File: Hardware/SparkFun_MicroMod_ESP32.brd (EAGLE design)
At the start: 22 x 22 mm, 55 parts, among them J1 MICROMOD-2222, Q2 MBT3904DW1T1, U1 W25QXX128MBIT-6X5, U2 ESP32, U4 CP2102N, Y1 40MHz, Y2 32.768kHz

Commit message: v10
- Updated board to v10
- Removed RX and TX test points
- Changed Flash_VDD label to VDD power symbol
- Changed SPI labels to COPI CIPO
- Added vias below antenna
- Moved OSHW logo
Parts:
- removed TP1, TP2: (no value), SparkFun-Connectors:PAD.03X.03
- moved LOGO3 3.68 mm to (16.0, 8.59)
- moved Q2 0.26 mm to (20.0, 9.69)
- moved R18 0.06 mm to (20.0, 11.7)
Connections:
- net 15-SPI_MOSI/SD_CMD renamed 15-SPI_COPI/SD_CMD
- net 2-SPI_MISO/SD_DATA0 renamed 2-SPI_CIPO/SD_DATA0
- net FLASH_VDD renamed VDD
- net U0RXD: no longer TP1.P$1
- net U0TXD: no longer TP2.P$1
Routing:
- net U0TXD: track 18.1 -> 12.5 mm
- net DTR: track 10.1 -> 9.01 mm
- net U0RXD: track 11.0 -> 10.2 mm
- net N$12: track 2.97 -> 3.50 mm
- net GND: vias 67 -> 71
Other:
- board text added: "v10"
- board text removed: "v02"

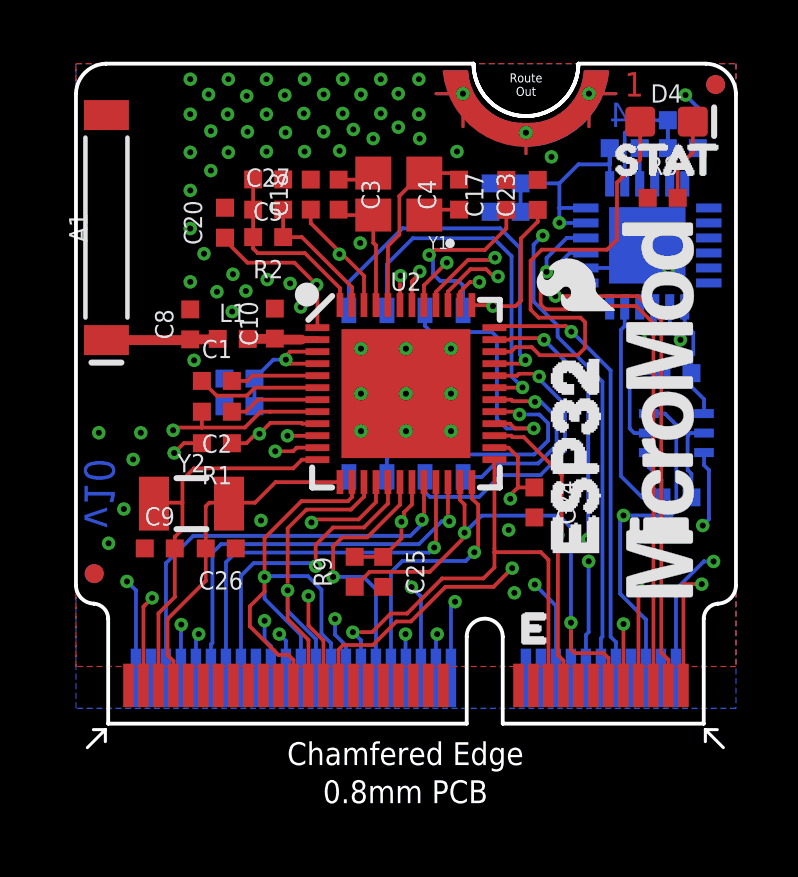
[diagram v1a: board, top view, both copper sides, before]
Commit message: v10 fix
Rearranged GPIO pins

-Boot was removed from I2C_INT
-GPIO4 was moved from G0 to I2C_INT
-GPIO12 was moved from G1 to G4
-Moved GPIO25/26 from G4/5 to G0/1
-Swapped GPIO16/17 from G2/3 to G3/2
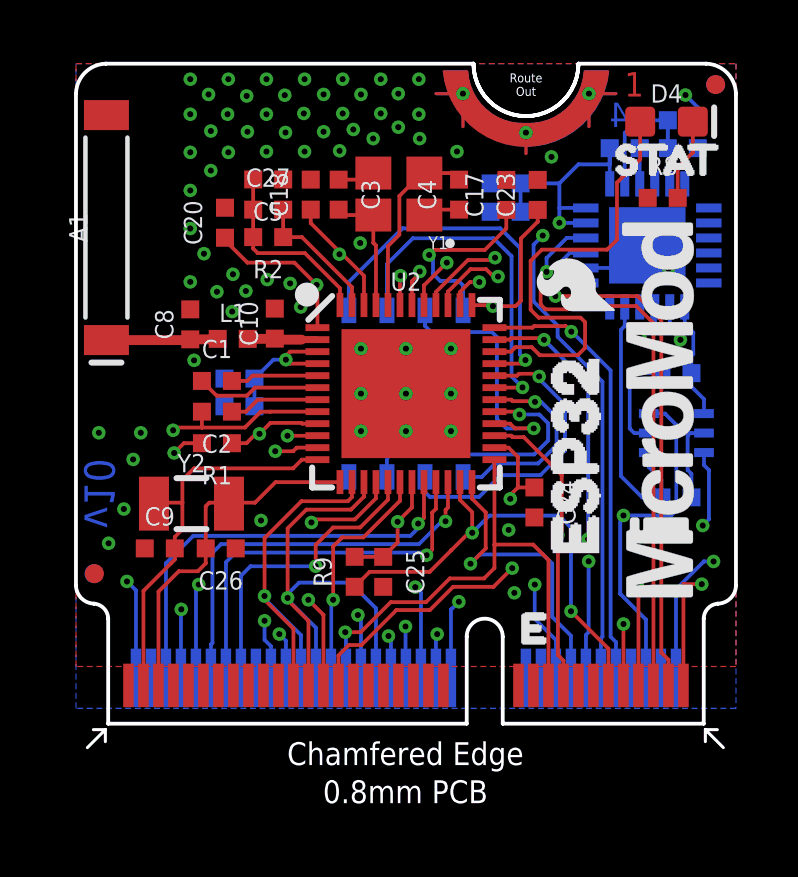
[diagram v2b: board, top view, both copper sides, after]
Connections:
- removed net 0-!BOOT!/I2C_!INT: J1.11, J1.16, Q2.6, R9.1, U2.23
- removed net 12-SD_DATA2/G1: J1.42, J1.68, U2.18
- removed net 16-G2/RX1/AUD_IN: J1.19, J1.44, J1.54, U2.25
- removed net 17-G3/TX1/AUD_OUT: J1.17, J1.46, J1.56, U2.27
- removed net 25-G4/AUD_LRCLK/SCL1: J1.48, J1.52, J1.53, U2.14
- removed net 26-G5/AUD_BCLK/SDA1: J1.50, J1.51, J1.73, U2.15
- removed net 32-G6/RTC: C9.2, J1.71, U2.12, Y2.P$1
- removed net 33-G7/RTC: C26.2, J1.69, U2.13, Y2.P$2
- removed net 4-SD_DATA1/G0: J1.40, J1.66, U2.24
- new net 0-!BOOT!: J1.11, Q2.6, R9.1, U2.23
- new net 12-SD_DATA2/G4: J1.48, J1.68, U2.18
- new net 16-G3/RX1/AUD_IN: J1.19, J1.46, J1.54, U2.25
- new net 17-G2/TX1/AUD_OUT: J1.17, J1.44, J1.56, U2.27
- new net 25-G0/AUD_LRCLK/SCL1: J1.40, J1.52, J1.53, U2.14
- new net 26-G1/AUD_BCLK/SDA1: J1.42, J1.50, J1.51, U2.15
- new net 32-G5/RTC: C9.2, J1.73, U2.12, Y2.P$1
- new net 33-G6/RTC: C26.2, J1.71, U2.13, Y2.P$2
- new net 4-SD_DATA1/I2C_!INT: J1.16, J1.66, U2.24
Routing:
- net 0-!BOOT!/I2C_!INT: track 26.7 -> 0.00 mm, vias 3 -> 0
- net 17-G2/TX1/AUD_OUT: track 0.00 -> 26.4 mm, vias 0 -> 3
- net 17-G3/TX1/AUD_OUT: track 25.6 -> 0.00 mm, vias 3 -> 0
- net 0-!BOOT!: track 0.00 -> 24.2 mm, vias 0 -> 3
- net 4-SD_DATA1/I2C_!INT: track 0.00 -> 23.4 mm, vias 0 -> 2
- net 26-G5/AUD_BCLK/SDA1: track 23.2 -> 0.00 mm, vias 2 -> 0
- net 4-SD_DATA1/G0: track 22.4 -> 0.00 mm, vias 2 -> 0
- net 16-G3/RX1/AUD_IN: track 0.00 -> 21.0 mm, vias 0 -> 2
- net 16-G2/RX1/AUD_IN: track 21.0 -> 0.00 mm, vias 2 -> 0
- net 12-SD_DATA2/G1: track 19.4 -> 0.00 mm, vias 2 -> 0
- net 25-G0/AUD_LRCLK/SCL1: track 0.00 -> 19.1 mm, vias 0 -> 2
- net 25-G4/AUD_LRCLK/SCL1: track 18.9 -> 0.00 mm, vias 1 -> 0
- net 26-G1/AUD_BCLK/SDA1: track 0.00 -> 17.9 mm, vias 0 -> 1
- net 12-SD_DATA2/G4: track 0.00 -> 16.0 mm, vias 0 -> 2
- net 32-G5/RTC: track 0.00 -> 13.1 mm
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
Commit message: Updated USB to UART
USB to UART converter can be either the CP2102N or CP2104
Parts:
- U4: value CP2102N -> CP210X
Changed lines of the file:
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@@
 <?xml version="1.0" encoding="utf-8"?>
 <!DOCTYPE eagle SYSTEM "eagle.dtd">
-<eagle version="9.6.2">
+<eagle version="9.5.2">
 <drawing>
 <settings>
@@
 <attribute name="VALUE" x="11" y="7.571" size="0.6096" layer="27" font="vector" ratio="20" align="top-center"/>
 </element>
-<element name="U4" library="SparkFun-IC-Comms" package="QFN24" value="CP2102N" x="19.044" y="15.9402" smashed="yes" rot="MR180">
+<element name="U4" library="SparkFun-IC-Comms" package="QFN24" value="CP210X" x="19.044" y="15.9402" smashed="yes" rot="MR180">
 <attribute name="NAME" x="18.155" y="15.5592" size="0.4064" layer="26" rot="MR180"/>
 <attribute name="PROD_ID" value="IC-14020" x="64.764" y="64.2002" size="1.778" layer="28" rot="MR180" display="off"/>

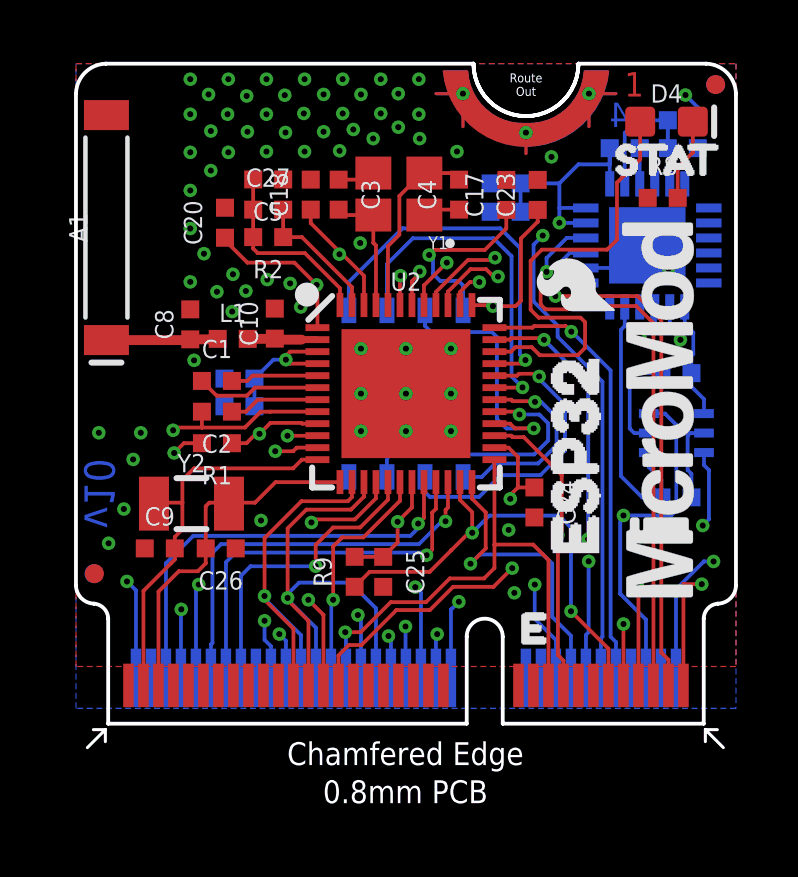
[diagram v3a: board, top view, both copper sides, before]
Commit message: v11
- Updated to new MicroMod Pinout
- Changed SCK from 14 to 18
- Changed SDO from 15 to 23
- Changed SDI from 2 to 19
- Changed CS from 13 to 5

- Changed PWM0 from 18 to 13
- Changed PWM1 from 19 to 12
- Changed D0 from 23 to 14

- Updated G0-G4 (mainly just changed GPIO12 to GPIO15, and moved that IO pin G4 to G0 and pushed the other IO pins down one position.
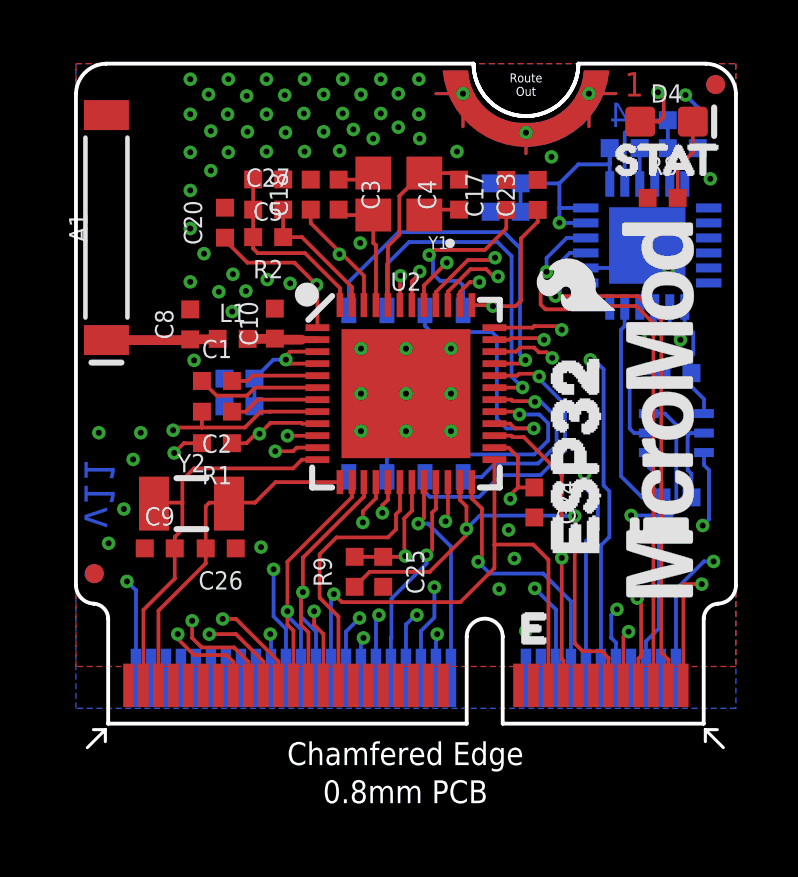
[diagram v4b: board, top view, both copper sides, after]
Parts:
- U4: value CP210X -> CP2102N
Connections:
- removed net 12-SD_DATA2/G4: J1.48, J1.68, U2.18
- removed net 13-SPI_!CS!/SD_DATA3: J1.70, U2.20
- removed net 14-SPI_SCK/SD_CLK: J1.60, U2.17
- removed net 15-SPI_COPI/SD_CMD: J1.62, U2.21
- removed net 16-G3/RX1/AUD_IN: J1.19, J1.46, J1.54, U2.25
- removed net 17-G2/TX1/AUD_OUT: J1.17, J1.44, J1.56, U2.27
- removed net 18-PWM0: J1.32, U2.35
- removed net 19-PWM1: J1.47, U2.38
- removed net 2-SPI_CIPO/SD_DATA0: J1.64, U2.22
- removed net 23-D0: J1.10, U2.36
- removed net 25-G0/AUD_LRCLK/SCL1: J1.40, J1.52, J1.53, U2.14
- removed net 26-G1/AUD_BCLK/SDA1: J1.42, J1.50, J1.51, U2.15
- removed net 4-SD_DATA1/I2C_!INT: J1.16, J1.66, U2.24
- removed net 5-STAT_LED: D4.A, U2.34
- new net 12-PWM1: J1.47, U2.18
- new net 13-PWM0: J1.32, U2.20
- new net 14-D0: J1.10, U2.17
- new net 15-G0: J1.40, U2.21
- new net 16-G4/RX1/AUD_IN: J1.19, J1.48, J1.54, U2.25
- new net 17-G3/TX1/AUD_OUT: J1.17, J1.46, J1.56, U2.27
- new net 18-SCK: J1.57, U2.35
- new net 19-CIPO: J1.61, U2.38
- new net 2-STAT_LED: D4.A, U2.22
- new net 23-COPI: J1.59, U2.36
- new net 25-G1/AUD_LRCLK/SCL1: J1.42, J1.52, J1.53, U2.14
- new net 26-G2/AUD_BCLK/SDA1: J1.44, J1.50, J1.51, U2.15
- new net 4-I2C_!INT: J1.16, U2.24
- new net 5-!CS: J1.55, U2.34
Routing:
- net 2-STAT_LED: track 0.00 -> 29.6 mm, vias 0 -> 2
- net 23-COPI: track 0.00 -> 27.1 mm, vias 0 -> 2
- net 17-G2/TX1/AUD_OUT: track 26.4 -> 0.00 mm, vias 3 -> 0
- net 18-SCK: track 0.00 -> 24.9 mm, vias 0 -> 2
- net 16-G4/RX1/AUD_IN: track 0.00 -> 24.9 mm, vias 0 -> 2
- net 5-!CS: track 0.00 -> 24.8 mm, vias 0 -> 2
- net 17-G3/TX1/AUD_OUT: track 0.00 -> 24.7 mm, vias 0 -> 3
- net 19-CIPO: track 0.00 -> 23.9 mm, vias 0 -> 2
- net 19-PWM1: track 23.9 -> 0.00 mm, vias 2 -> 0
- net 4-SD_DATA1/I2C_!INT: track 23.4 -> 0.00 mm, vias 2 -> 0
- net 16-G3/RX1/AUD_IN: track 21.0 -> 0.00 mm, vias 2 -> 0
- net 25-G0/AUD_LRCLK/SCL1: track 19.1 -> 0.00 mm, vias 2 -> 0
- net 26-G2/AUD_BCLK/SDA1: track 0.00 -> 18.9 mm, vias 0 -> 2
- net 26-G1/AUD_BCLK/SDA1: track 17.9 -> 0.00 mm, vias 1 -> 0
- net 18-PWM0: track 17.3 -> 0.00 mm, vias 3 -> 0
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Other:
- board text added: "v11"
- board text removed: "v10"

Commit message: v11 update
- Added notes to boot strapping pins
- Added ENIG finish note to tDocu
- Updated labeling for USB to UART brdige
- Updated SPI flash labels
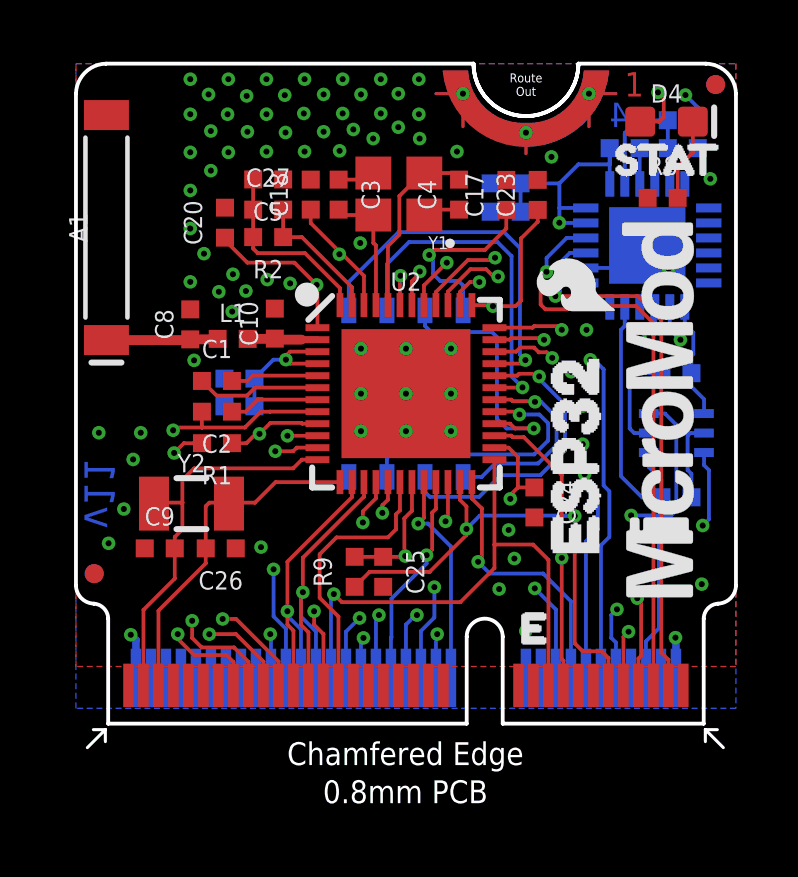
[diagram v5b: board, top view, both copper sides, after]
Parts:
- U4: value CP2102N -> CP210X
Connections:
- net FLASH_SD_CLK renamed FLASH_SCK
- net FLASH_SD_CMD renamed FLASH_SCS
- net FLASH_SD_DATA0 renamed FLASH_SDO
- net FLASH_SD_DATA1 renamed FLASH_SDI
- net FLASH_SD_DATA2 renamed FLASH_SHD
- net FLASH_SD_DATA3 renamed FLASH_SWP
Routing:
- net 3.3V: track 42.0 -> 36.9 mm
- net GND: track 16.4 -> 12.4 mm, vias 73 -> 77
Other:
- board text added: "0.8mm PCB ENIG Finish 45 degree chamfered edge Four layer design"
- board text removed: "0.8mm PCB 45 degree chamfered edge Four layer design"
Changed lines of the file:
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@@
 <?xml version="1.0" encoding="utf-8"?>
 <!DOCTYPE eagle SYSTEM "eagle.dtd">
-<eagle version="9.6.2">
+<eagle version="9.5.2">
 <drawing>
 <settings>
@@
 <setting verticaltext="up"/>
 </settings>
-<grid distance="0.05" unitdist="inch" unit="inch" style="lines" multiple="1" display="yes" altdistance="0.0025" altunitdist="inch" altunit="inch"/>
+<grid distance="0.05" unitdist="inch" unit="inch" style="lines" multiple="1" display="yes" altdistance="0.005" altunitdist="inch" altunit="inch"/>
 <layers>
 <layer number="1" name="Top" color="4" fill="1" visible="yes" active="yes"/>
@@
 <layer number="19" name="Unrouted" color="6" fill="1" visible="yes" active="yes"/>
 <layer number="20" name="Dimension" color="24" fill="1" visible="yes" active="yes"/>
-<layer number="21" name="tPlace" color="58" fill="1" visible="no" active="yes"/>
-<layer number="22" name="bPlace" color="14" fill="1" visible="no" active="yes"/>
-<layer number="23" name="tOrigins" color="15" fill="1" visible="no" active="yes"/>
-<layer number="24" name="bOrigins" color="15" fill="1" visible="no" active="yes"/>
+<layer number="21" name="tPlace" color="16" fill="1" visible="yes" active="yes"/>
+<layer number="22" name="bPlace" color="14" fill="1" visible="yes" active="yes"/>
+<layer number="23" name="tOrigins" color="15" fill="1" visible="yes" active="yes"/>
+<layer number="24" name="bOrigins" color="15" fill="1" visible="yes" active="yes"/>
 <layer number="25" name="tNames" color="7" fill="1" visible="no" active="yes"/>
 <layer number="26" name="bNames" color="7" fill="1" visible="no" active="yes"/>
@@
 <layer number="43" name="vRestrict" color="2" fill="10" visible="no" active="yes"/>
 <layer number="44" name="Drills" color="7" fill="1" visible="no" active="yes"/>
-<layer number="45" name="Holes" color="7" fill="1" visible="no" active="yes"/>
+<layer number="45" name="Holes" color="7" fill="1" visible="yes" active="yes"/>
 <layer number="46" name="Milling" color="3" fill="1" visible="no" active="yes"/>
 <layer number="47" name="Measures" color="7" fill="1" visible="no" active="yes"/>
@@
 <layer number="49" name="Reference" color="7" fill="1" visible="no" active="yes"/>
 <layer number="50" name="dxf" color="7" fill="1" visible="no" active="yes"/>
-<layer number="51" name="tDocu" color="6" fill="1" visible="no" active="yes"/>
+<layer number="51" name="tDocu" color="6" fill="1" visible="yes" active="yes"/>
 <layer number="52" name="bDocu" color="7" fill="1" visible="no" active="yes"/>
 <layer number="91" name="Nets" color="2" fill="1" visible="no" active="no"/>
@@
 <wire x1="0" y1="21" x2="1" y2="22" width="0.127" layer="20" curve="-87.205638"/>
 <wire x1="16.75" y1="22" x2="13.25" y2="22" width="0.127" layer="20" curve="-180"/>
-<text x="31.75" y="33.02" size="1.778" layer="51" font="vector" ratio="15">0.8mm PCB
+<text x="31.75" y="31.75" size="1.778" layer="51" font="vector" ratio="15">0.8mm PCB
+ENIG Finish
 45 degree chamfered edge
 Four layer design</text>
@@
 <attribute name="VALUE" x="11" y="7.571" size="0.6096" layer="27" font="vector" ratio="20" align="top-center"/>
 </element>
-<element name="U4" library="SparkFun-IC-Comms" package="QFN24" value="CP2102N" x="19.044" y="15.9402" smashed="yes" rot="MR180">
+<element name="U4" library="SparkFun-IC-Comms" package="QFN24" value="CP210X" x="19.044" y="15.9402" smashed="yes" rot="MR180">
 <attribute name="NAME" x="18.155" y="15.5592" size="0.4064" layer="26" rot="MR180"/>
 <attribute name="PROD_ID" value="IC-14020" x="64.764" y="64.2002" size="1.778" layer="28" rot="MR180" display="off"/>
@@
 <wire x1="7.138" y1="12.4" x2="6.997" y2="12.259" width="0.127" layer="1"/>
 <wire x1="6.997" y1="12.259" x2="6.997" y2="12.132" width="0.127" layer="1"/>
-<wire x1="20" y1="4.4776" x2="20" y2="1.525" width="0.127" layer="16"/>
-<wire x1="20.9292" y1="5.4068" x2="20" y2="4.4776" width="0.127" layer="16"/>
-<wire x1="20.9292" y1="5.4068" x2="21.2538" y2="5.4068" width="0.127" layer="16"/>
-<via x="21.2538" y="5.4068" extent="1-16" drill="0.2"/>
+<wire x1="20" y1="2.8668" x2="20" y2="1.525" width="0.254" layer="16"/>
+<wire x1="20" y1="2.8668" x2="19.9838" y2="2.8668" width="0.254" layer="16"/>
+<via x="19.9838" y="2.8668" extent="1-16" drill="0.2"/>
 <wire x1="16.994" y1="16.6902" x2="16.1184" y2="16.6902" width="0.127" layer="16"/>
 <wire x1="16.113" y1="16.6956" x2="16.1184" y2="16.6902" width="0.127" layer="16"/>
 <wire x1="17.794" y1="17.9902" x2="17.792" y2="17.9902" width="0.127" layer="16"/>
 <wire x1="17.792" y1="17.9902" x2="17.792" y2="19.183" width="0.127" layer="16"/>
-<wire x1="2" y1="1.525" x2="2" y2="4.441" width="0.127" layer="16"/>
-<wire x1="2" y1="4.441" x2="1.7" y2="4.741" width="0.127" layer="16"/>
-<via x="1.7" y="4.741" extent="1-16" drill="0.2"/>
+<wire x1="2" y1="1.525" x2="2" y2="2.79" width="0.254" layer="16"/>
+<wire x1="2" y1="2.79" x2="1.827" y2="2.963" width="0.254" layer="16"/>
+<via x="1.827" y="2.963" extent="1-16" drill="0.2"/>
 <wire x1="8.7808" y1="15.6468" x2="8.7808" y2="15.7302" width="0.127" layer="1"/>
 <wire x1="8.7808" y1="15.7302" x2="7.826" y2="16.685" width="0.127" layer="1"/>
@@
 <vertex x="22" y="0.508"/>
 </polygon>
-<wire x1="20.25" y1="1.275" x2="20.25" y2="4.65" width="0.127" layer="1"/>
-<wire x1="20.25" y1="4.65" x2="20.86" y2="4.65" width="0.127" layer="1"/>
 <via x="20.86" y="4.65" extent="1-16" drill="0.2"/>
 <via x="18.71" y="4.182" extent="1-16" drill="0.2"/>
@@
 <via x="14.1055" y="4.487" extent="1-16" drill="0.2"/>
 <via x="21.1455" y="18.161" extent="1-16" drill="0.2"/>
+<via x="17.0182" y="13.1256" extent="1-16" drill="0.2"/>
+<via x="16.5102" y="11.7286" extent="1-16" drill="0.2"/>
+<via x="16.8912" y="10.5856" extent="1-16" drill="0.2"/>
+<via x="16.8912" y="9.3156" extent="1-16" drill="0.2"/>
 </signal>
 <signal name="32-G5/RTC">
@@
 <wire x1="5.907" y1="18.139" x2="5.907" y2="17.133" width="0.127" layer="1"/>
 </signal>
-<signal name="FLASH_SD_DATA3">
+<signal name="FLASH_SWP">
 <contactref element="U2" pad="29"/>
 <contactref element="U1" pad="3"/>
@@
 <wire x1="10.497" y1="8.973" x2="15.273" y2="8.973" width="0.127" layer="16"/>
 </signal>
-<signal name="FLASH_SD_DATA2">
+<signal name="FLASH_SHD">
 <contactref element="U2" pad="28"/>
 <contactref element="U1" pad="7"/>
@@
 <wire x1="11.635" y1="13.257" x2="11.635" y2="13.775" width="0.127" layer="16"/>
 </signal>
-<signal name="FLASH_SD_DATA1">
+<signal name="FLASH_SDI">
 <contactref element="U2" pad="33"/>
 <contactref element="U1" pad="5"/>
@@
 <wire x1="9.095" y1="14.725" x2="9.095" y2="13.775" width="0.127" layer="16"/>
 </signal>
-<signal name="FLASH_SD_DATA0">
+<signal name="FLASH_SDO">
 <contactref element="U2" pad="32"/>
 <contactref element="U1" pad="2"/>
@@
 <wire x1="14.1628" y1="8.2828" x2="15.4793875" y2="8.2828" width="0.127" layer="16"/>
 </signal>
-<signal name="FLASH_SD_CLK">
+<signal name="FLASH_SCK">
 <contactref element="U2" pad="31"/>
 <contactref element="U1" pad="6"/>
@@
 <wire x1="11.1016" y1="16.053" x2="10.365" y2="15.3164" width="0.127" layer="16"/>
 </signal>
-<signal name="FLASH_SD_CMD">
+<signal name="FLASH_SCS">
 <contactref element="U2" pad="30"/>
 <contactref element="U1" pad="1"/>
